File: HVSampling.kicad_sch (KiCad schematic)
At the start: 52 parts, among them K4 SPU01M-05, U5 AMC1351DWV, U6 AMC1351DWV, U7 LM393, U8 4N35, U9 TLV6002

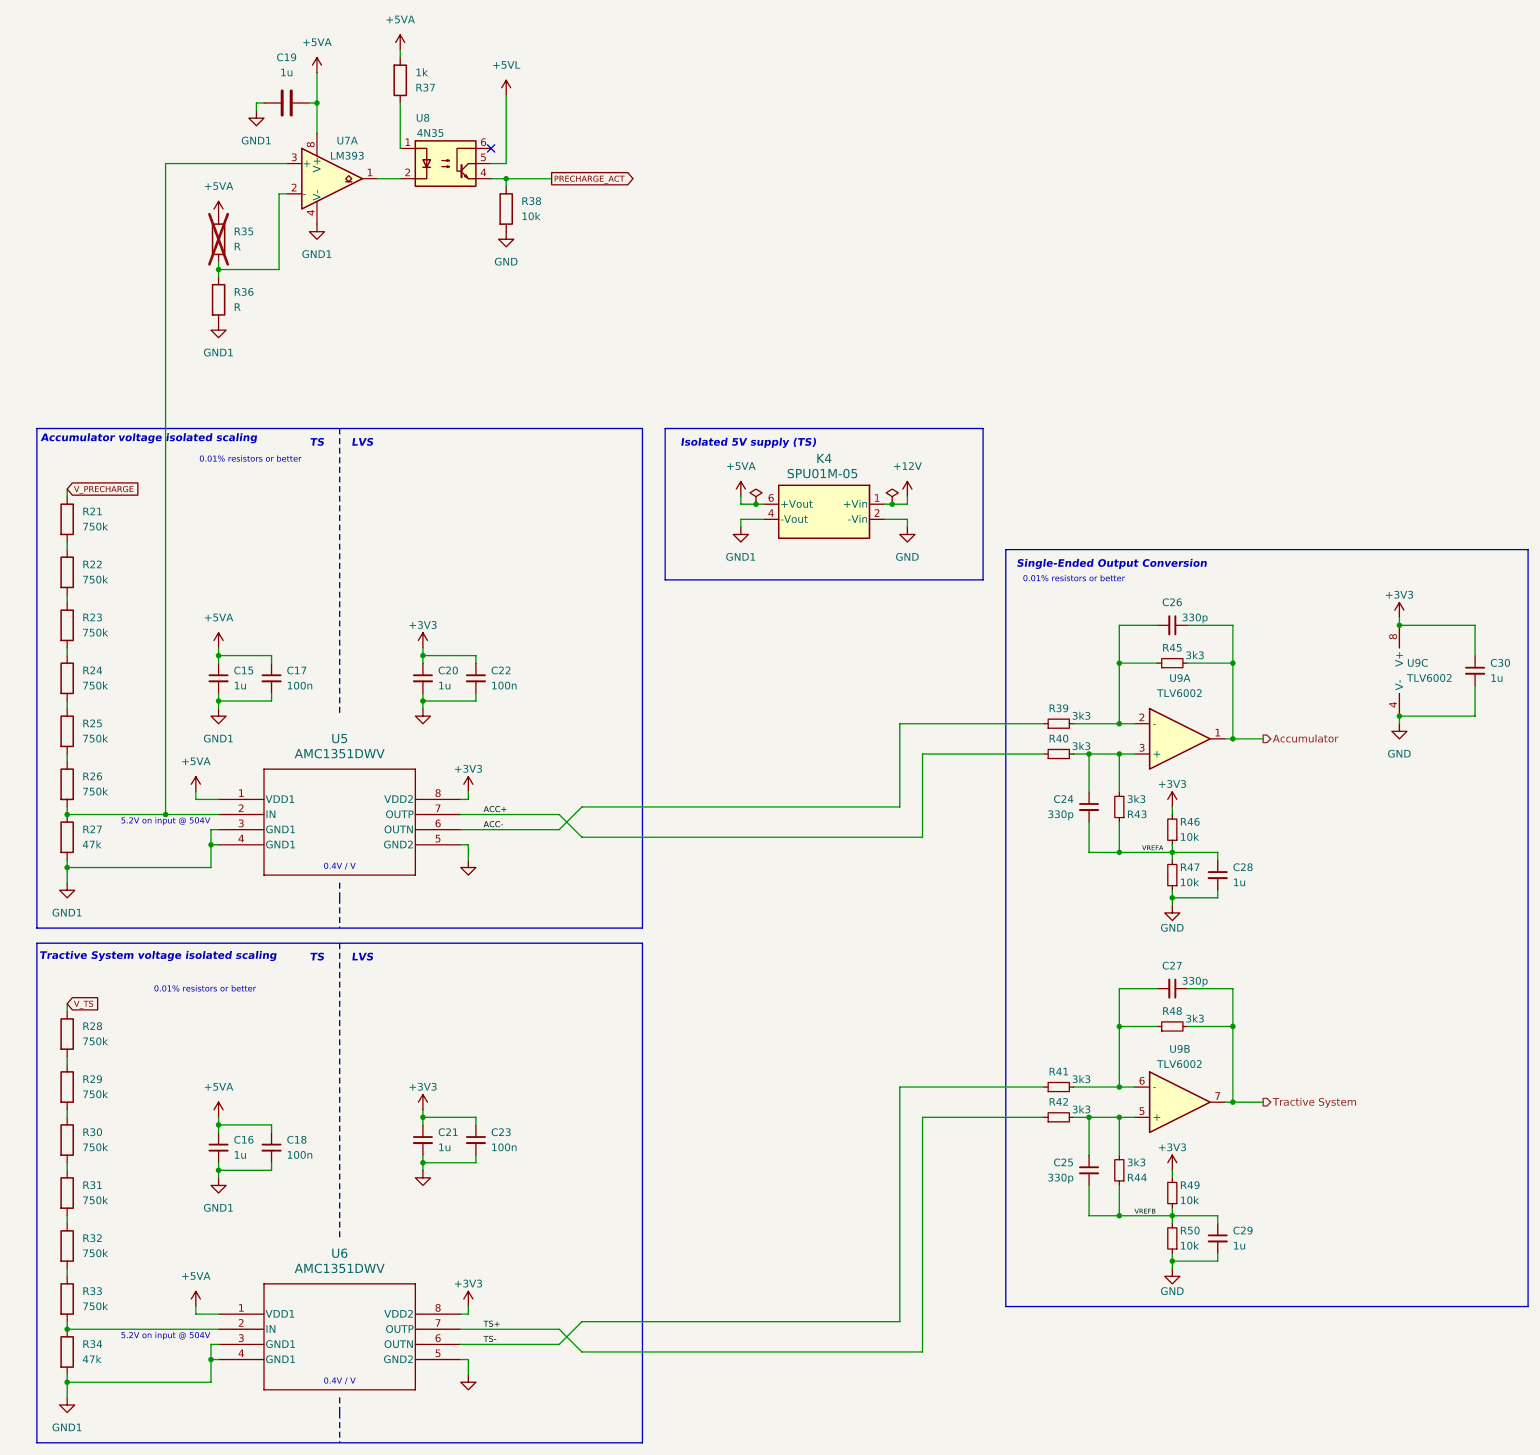
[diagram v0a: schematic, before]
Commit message: *: Use kicad-library exclusively
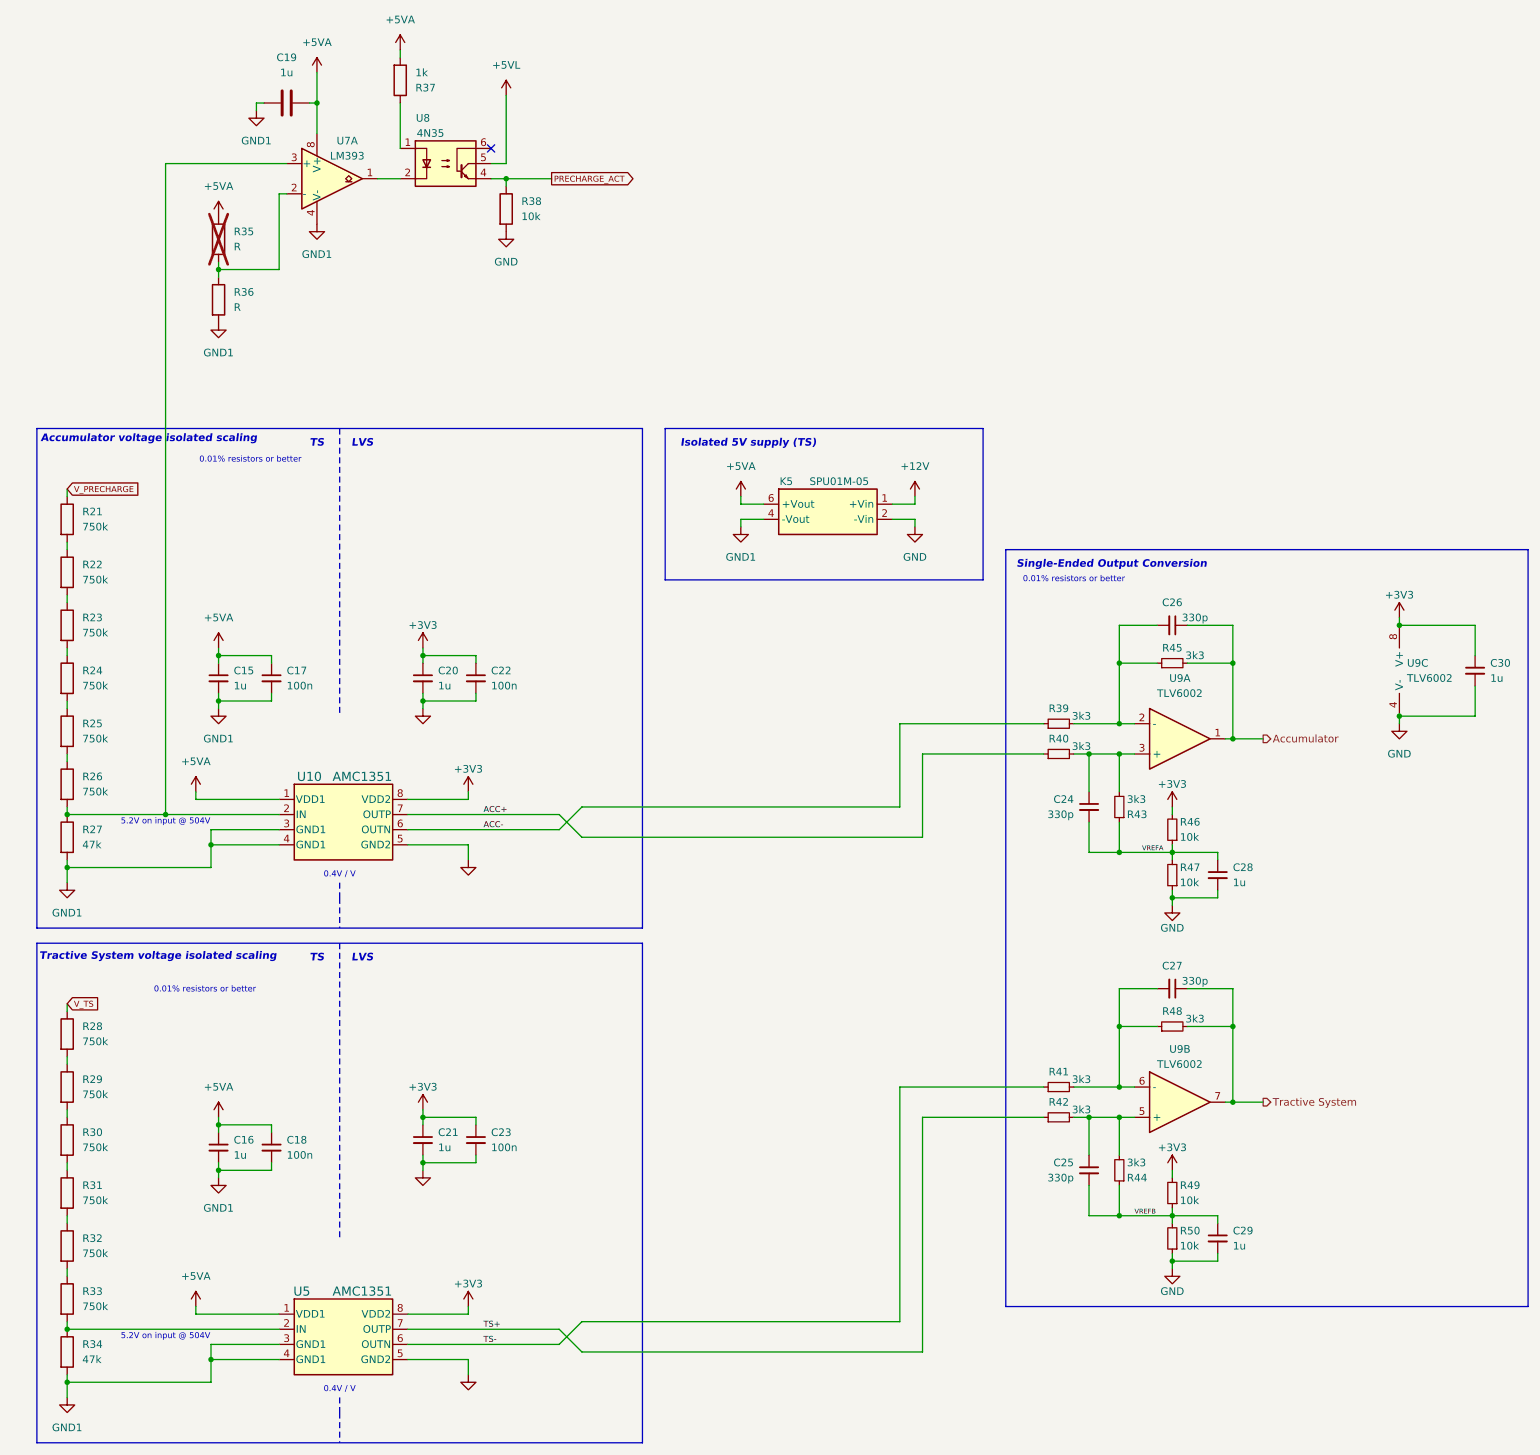
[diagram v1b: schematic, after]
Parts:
- removed K4: SPU01M-05, MyLibrary:DPU01M05, symbol SPU01M-05:SPU01M-05
- removed U5, U6: AMC1351DWV, Package_SO:SOIC-8_3.9x4.9mm_P1.27mm, symbol AMC1351:AMC1351DWV
- added K5: SPU01M-05, symbol yfs:SPU01M-05
- added U10, U5: AMC1351, Package_SO:SOIC-8_3.9x4.9mm_P1.27mm, symbol yfs:AMC1351
- U9: symbol Components:TLV6002 -> yfs:TLV6002
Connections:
- net +12V: now also K5.1 (+Vin)
- net +3V3: now also U10.8 (VDD2), U5.8 (VDD2)
- net +5VA: now also K5.6 (+Vout), U10.1 (VDD1), U5.1 (VDD1)
- net ACC+: now also U10.7 (OUTP)
- net ACC-: now also U10.6 (OUTN)
- net GND: now also K5.2 (-Vin), U10.5 (GND2), U5.5 (GND2)
- net GND1: now also K5.4 (-Vout), U10.3 (GND1), U10.4 (GND1), U5.3 (GND1), U5.4 (GND1)
- net TS+: now also U5.7 (OUTP)
- net TS-: now also U5.6 (OUTN)
- net at R33.2, R34.1: now also U5.2 (IN)
- net at R26.2, R27.1, U7.3 (+): now also U10.2 (IN)

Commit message: schematic: Tie unused LM393 inputs low
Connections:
- net GND1: now also U7.5 (+), U7.6 (-)
- no-connect marks 1 -> 2
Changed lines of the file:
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@@
 	)
 	(junction
+		(at 120.65 -40.64)
+		(diameter 0)
+		(color 0 0 0 0)
+	)
+	(junction
 		(at 196.85 86.36)
 		(diameter 0)
@@
 		(at 91.44 -31.75)
 	)
+	(no_connect
+		(at 137.16 -43.18)
+	)
 	(polyline
 		(pts
@@
 	(wire
 		(pts
+			(xy 120.65 -40.64) (xy 120.65 -45.72)
+		)
+		(stroke
+			(width 0)
+			(type default)
+		)
+	)
+	(wire
+		(pts
 			(xy 93.98 -29.21) (xy 91.44 -29.21)
 		)
@@
 	(wire
 		(pts
+			(xy 120.65 -39.37) (xy 120.65 -40.64)
+		)
+		(stroke
+			(width 0)
+			(type default)
+		)
+	)
+	(wire
+		(pts
 			(xy 196.85 54.61) (xy 196.85 64.77)
 		)
@@
 	(wire
 		(pts
+			(xy 120.65 -45.72) (xy 121.92 -45.72)
+		)
+		(stroke
+			(width 0)
+			(type default)
+		)
+	)
+	(wire
+		(pts
 			(xy 20.32 34.29) (xy 20.32 35.56)
 		)
@@
 	(wire
 		(pts
+			(xy 120.65 -40.64) (xy 121.92 -40.64)
+		)
+		(stroke
+			(width 0)
+			(type default)
+		)
+	)
+	(wire
+		(pts
 			(xy 41.91 162.56) (xy 41.91 163.83)
 		)
@@
 	)
 	(symbol
-		(lib_name "LM393_1")
+		(lib_name "LM393_2")
 		(lib_id "Comparator:LM393")
 		(at 64.77 -26.67 0)
@@
 	)
 	(symbol
+		(lib_name "LM393_1")
+		(lib_id "Comparator:LM393")
+		(at 129.54 -43.18 0)
+		(unit 2)
+		(exclude_from_sim no)
+		(in_bom yes)
+		(on_board yes)
+		(dnp no)
+		(fields_autoplaced yes)
+		(property "Reference" "U7"
+			(at 129.54 -52.07 0)
+			(effects
+				(font
+					(size 1.27 1.27)
+				)
+			)
+		)
+		(property "Value" "LM393"
+			(at 129.54 -49.53 0)
+			(effects
+				(font
+					(size 1.27 1.27)
+				)
+			)
+		)
+		(property "Footprint" "Package_SO:SOIC-8_3.9x4.9mm_P1.27mm"
+			(at 129.54 -43.18 0)
+			(effects
+				(font
+					(size 1.27 1.27)
+				)
+				(hide yes)
+			)
+		)
+		(property "Datasheet" "http://www.ti.com/lit/ds/symlink/lm393.pdf"
+			(at 129.54 -43.18 0)
+			(effects
+				(font
+					(size 1.27 1.27)
+				)
+				(hide yes)
+			)
+		)
+		(property "Description" "Low-Power, Low-Offset Voltage, Dual Comparators, DIP-8/SOIC-8/TO-99-8"
+			(at 129.54 -43.18 0)
+			(effects
+				(font
+					(size 1.27 1.27)
+				)
+				(hide yes)
+			)
+		)
+		(pin "1"
+		)
+		(pin "2"
+		)
+		(pin "3"
+		)
+		(pin "5"
+		)
+		(pin "6"
+		)
+		(pin "7"
+		)
+		(pin "4"
+		)
+		(pin "8"
+		)
+		(instances
+			(project "Precharge_PCB"
+				(path "/c467677d-b98c-4488-bd11-965ef67263b2/5111e28e-8231-41c0-b506-a567affaf28a"
+					(reference "U7")
+					(unit 2)
+				)
+			)
+		)
+	)
+	(symbol
 		(lib_id "power:GND")
 		(at 205.74 156.21 0)
@@
 	)
 	(symbol
+		(lib_id "power:GND1")
+		(at 120.65 -39.37 0)
+		(unit 1)
+		(exclude_from_sim no)
+		(in_bom yes)
+		(on_board yes)
+		(dnp no)
+		(fields_autoplaced yes)
+		(property "Reference" "#PWR094"
+			(at 120.65 -33.02 0)
+			(effects
+				(font
+					(size 1.27 1.27)
+				)
+				(hide yes)
+			)
+		)
+		(property "Value" "GND1"
+			(at 120.65 -34.29 0)
+			(effects
+				(font
+					(size 1.27 1.27)
+				)
+			)
+		)
+		(property "Footprint" ""
+			(at 120.65 -39.37 0)
+			(effects
+				(font
+					(size 1.27 1.27)
+				)
+				(hide yes)
+			)
+		)
+		(property "Datasheet" ""
+			(at 120.65 -39.37 0)
+			(effects
+				(font
+					(size 1.27 1.27)
+				)
+				(hide yes)
+			)
+		)
+		(property "Description" "Power symbol creates a global label with name \"GND1\" , ground"
+			(at 120.65 -39.37 0)
+			(effects
+				(font
+					(size 1.27 1.27)
+				)
+				(hide yes)
+			)
+		)
+		(pin "1"
+		)
+		(instances
+			(project "Precharge_PCB"
+				(path "/c467677d-b98c-4488-bd11-965ef67263b2/5111e28e-8231-41c0-b506-a567affaf28a"
+					(reference "#PWR094")
+					(unit 1)
+				)
+			)
+		)
+	)
+	(symbol
 		(lib_id "Device:C_Small")
 		(at 205.74 109.22 270)
@@
 			)
 		)
-		(property "Description" ""
+		(property "Description" "Optocoupler, Phototransistor Output, with Base Connection, Vce 70V, CTR 100%, Viso 5000V, DIP6"
 			(at 83.82 -29.21 0)
 			(effects

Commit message: schematic: Connect relay actual states to the MCU
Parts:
- added unit 2 of U7
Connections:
- net GND1: now also U7.5 (+), U7.6 (-); no longer U7.5 (+), U7.6 (-)
